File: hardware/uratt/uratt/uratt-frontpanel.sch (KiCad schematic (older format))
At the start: 17 parts

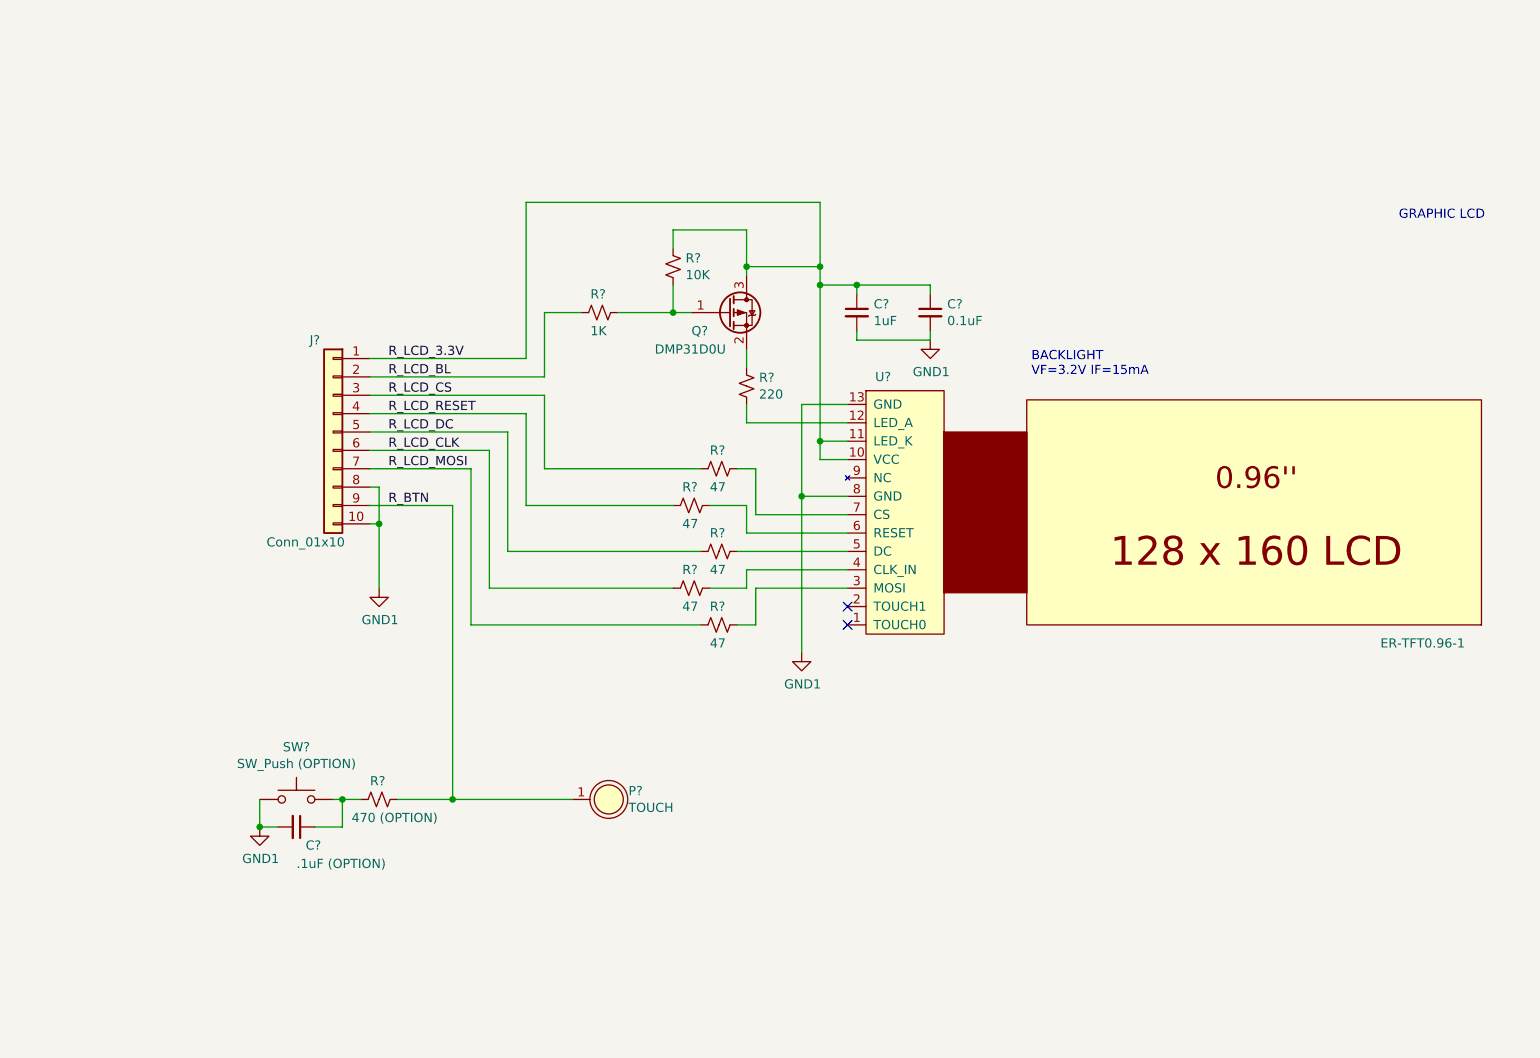
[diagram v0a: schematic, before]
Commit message: uRATT rough footprint assignment and placement for fitment
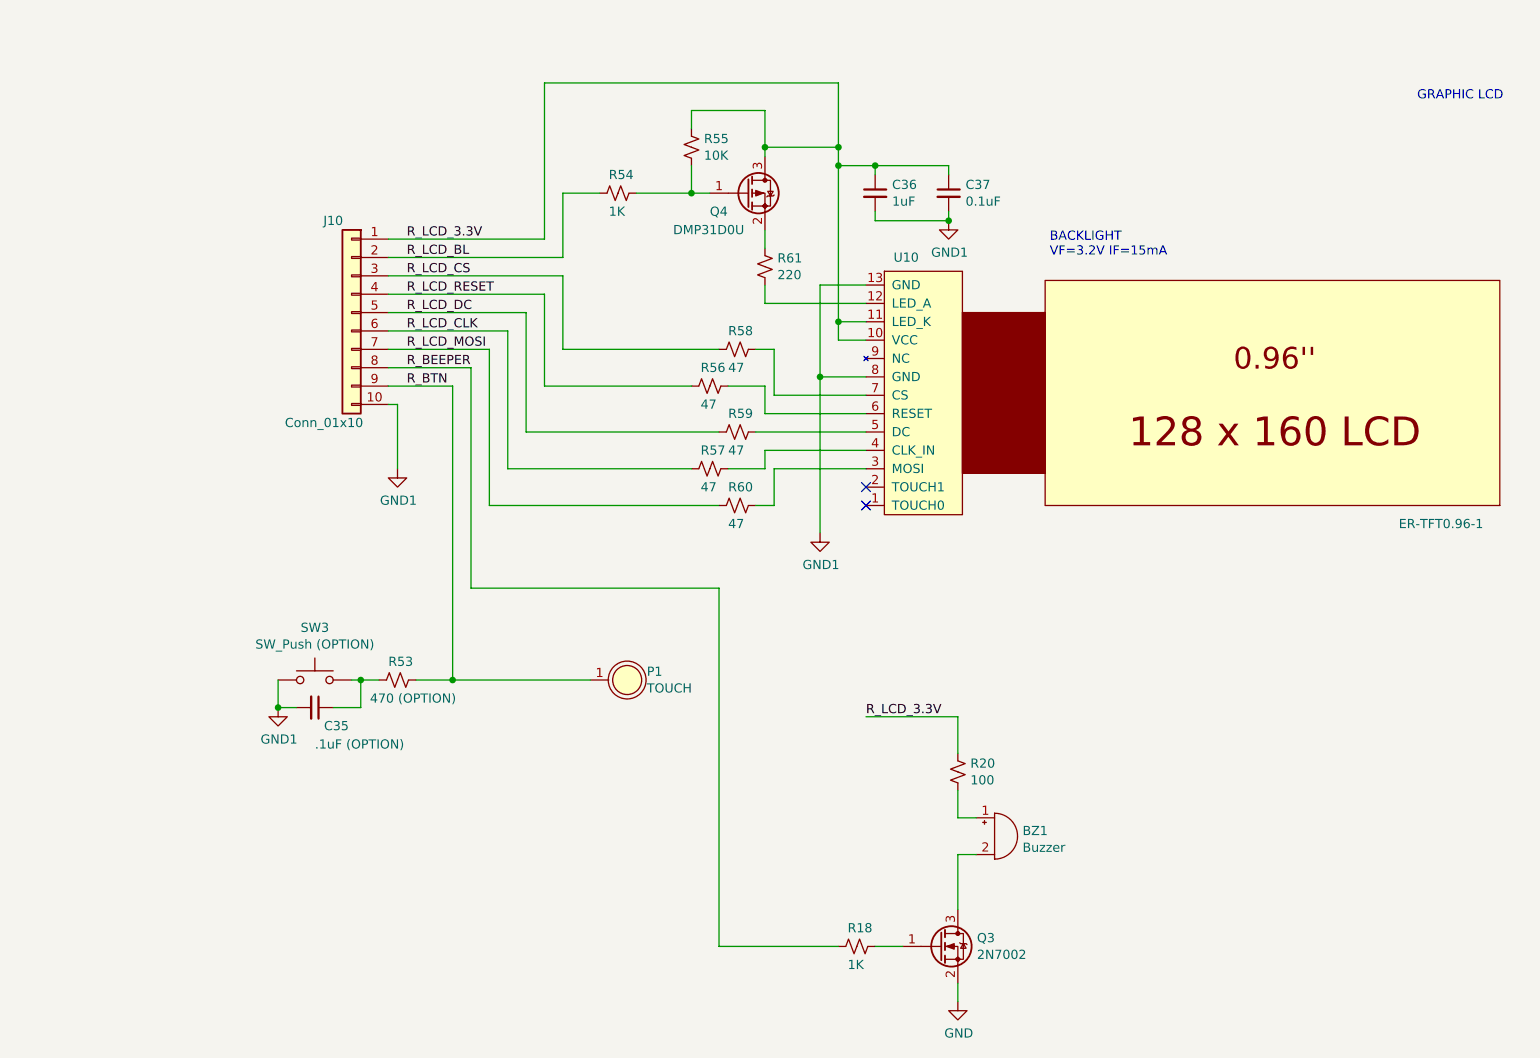
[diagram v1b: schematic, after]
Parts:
- added BZ1: Buzzer, Buzzer_Beeper:Buzzer_CUI_CPT-9019S-SMT, symbol Device:Buzzer
- added Q3: 2N7002, Package_TO_SOT_SMD:SOT-23, symbol Transistor_FET:2N7002
- added R18: 1K, Resistor_SMD:R_0603_1608Metric, symbol Device:R_Small_US
- added R20: 100, Resistor_SMD:R_0603_1608Metric, symbol Device:R_Small_US
- C35, C36, C37: renamed from C?; footprint (none) -> Capacitor_SMD:C_0603_1608Metric
- J10: renamed from J?; footprint (none) -> Connector_PinHeader_2.54mm:PinHeader_1x10_P2.54mm_Vertical
- P1: renamed from P?; footprint (none) -> TestPoint:TestPoint_Pad_4.0x4.0mm
- R53, R54, R55, R56, R57, R58, R59, R60, R61: renamed from R?; footprint (none) -> Resistor_SMD:R_0603_1608Metric
- SW3: renamed from SW?; footprint (none) -> Button_Switch_SMD:SW_Push_1P1T_NO_CK_KMR2
- gave numbers to parts that had none: 2
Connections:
- net GND1: no longer J10.8 (Pin_8)
- net R_LCD_3.3V: now also R20.1
- new net: BZ1.1 (-), R20.2
- new net: BZ1.2 (+), Q3.3 (D)
- new net: Q3.1 (G), R18.1
- new net GND: Q3.2 (S)
- new net R_BEEPER: J10.8 (Pin_8), R18.2
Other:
- moved on the sheet: C35, C36, C37, J10, P1, Q4, R53, R54, R55, R56, R57, R58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

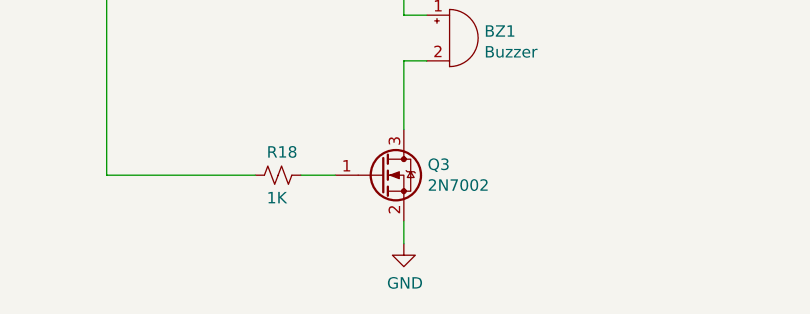
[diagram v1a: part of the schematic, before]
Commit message: import actual board outline DXF and adjust rough placement
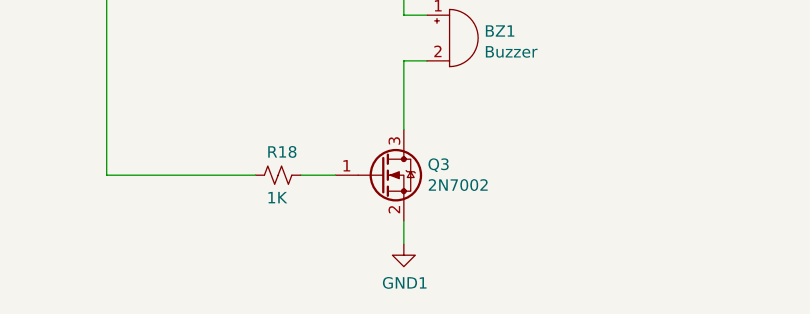
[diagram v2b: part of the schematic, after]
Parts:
- J10: footprint Connector_PinHeader_2.54mm:PinHeader_1x10_P2.54mm_Vertical -> Connector_PinHeader_2.00mm:PinHeader_1x10_P2.00mm_Vertical
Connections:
- net GND is gone; now on net GND1: Q3.2 (S)
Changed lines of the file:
@@
 F 0 "J10" H 3000 3150 50  0000 C CNN
 F 1 "Conn_01x10" H 3050 2050 50  0000 C CNN
-F 2 "Connector_PinHeader_2.54mm:PinHeader_1x10_P2.54mm_Vertical" H 2900 2650 50  0001 C CNN
+F 2 "Connector_PinHeader_2.00mm:PinHeader_1x10_P2.00mm_Vertical" H 2900 2650 50  0001 C CNN
 F 3 "~" H 2900 2650 50  0001 C CNN
 	1    2900 2650
@@
 	1    0    0    -1
 $EndComp
-$Comp
-L power:GND #PWR?
-U 1 1 60451D87
-P 6200 6400
-AR Path="/60451D87" Ref="#PWR?"  Part="1"
-AR Path="/62EF036B/60451D87" Ref="#PWR023"  Part="1"
-F 0 "#PWR023" H 6200 6150 50  0001 C CNN
-F 1 "GND" H 6205 6227 50  0000 C CNN
-F 2 "" H 6200 6400 50  0001 C CNN
-F 3 "" H 6200 6400 50  0001 C CNN
-	1    6200 6400
-	1    0    0    -1
-$EndComp
 Wire Wire Line
 	6200 6400 6200 6300
@@
 	6200 4850 6200 5050
 Connection ~ 6150 2150
+$Comp
+L power:GND1 #PWR?
+U 1 1 5FE7C0E9
+P 6200 6400
+AR Path="/5FE7C0E9" Ref="#PWR?"  Part="1"
+AR Path="/62EF036B/5FE7C0E9" Ref="#PWR?"  Part="1"
+F 0 "#PWR?" H 6200 6150 50  0001 C CNN
+F 1 "GND1" H 6205 6227 50  0000 C CNN
+F 2 "" H 6200 6400 50  0001 C CNN
+F 3 "" H 6200 6400 50  0001 C CNN
+	1    6200 6400
+	1    0    0    -1
+$EndComp
 $EndSCHEMATC

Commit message: WIP routing
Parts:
- added H5, H6, H7, H8: MountingHole, MountingHole:MountingHole_2.7mm_M2.5, symbol Mechanical:MountingHole
- J9: renamed from J10; footprint Connector_PinHeader_2.00mm:PinHeader_1x10_P2.00mm_Vertical -> Connector_FFC-FPC:TE_1-1734839-0_1x10-1MP_P0.5mm_Horizontal
- LCD1: renamed from U10; footprint (none) -> uratt:ER-TFT0.96-1
- renumbered C35 to C32, C36 to C33, C37 to C34, Q4 to Q3, Q3 to Q4, R53 to R43, R54 to R44, R55 to R45, R56 to R46, R57 to R47, R58 to R48, R59 to R49, R60 to R50, R61 to R51, R18 to R52, R20 to R53
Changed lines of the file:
@@
 $EndDescr
 $Comp
-L uratt:ER-TFT0.96-1 U?
+L uratt:ER-TFT0.96-1 LCD?
 U 1 1 62F12C4B
 P 5800 2300
-AR Path="/62F12C4B" Ref="U?"  Part="1"
-AR Path="/62EF036B/62F12C4B" Ref="U10"  Part="1"
-F 0 "U10" H 5850 2250 50  0000 L CNN
+AR Path="/62F12C4B" Ref="LCD?"  Part="1"
+AR Path="/62EF036B/62F12C4B" Ref="LCD1"  Part="1"
+F 0 "LCD1" H 5800 2250 50  0000 L CNN
 F 1 "ER-TFT0.96-1" H 8600 800 50  0000 L CNN
-F 2 "" H 5750 2375 50  0001 C CNN
+F 2 "uratt:ER-TFT0.96-1" H 5750 2375 50  0001 C CNN
 F 3 "https://www.buydisplay.com/download/manual/ER-TFT0.96-1_Datasheet.pdf" H 5750 2375 50  0001 C CNN
 	1    5800 2300
@@
 P 6150 2000
 AR Path="/62F12C53" Ref="C?"  Part="1"
-AR Path="/62EF036B/62F12C53" Ref="C37"  Part="1"
-F 0 "C37" H 6242 2046 50  0000 L CNN
+AR Path="/62EF036B/62F12C53" Ref="C34"  Part="1"
+F 0 "C34" H 6242 2046 50  0000 L CNN
 F 1 "0.1uF" H 6242 1955 50  0000 L CNN
 F 2 "Capacitor_SMD:C_0603_1608Metric" H 6150 2000 50  0001 C CNN
@@
 P 5750 2000
 AR Path="/62F12C5A" Ref="C?"  Part="1"
-AR Path="/62EF036B/62F12C5A" Ref="C36"  Part="1"
-F 0 "C36" H 5842 2046 50  0000 L CNN
+AR Path="/62EF036B/62F12C5A" Ref="C33"  Part="1"
+F 0 "C33" H 5842 2046 50  0000 L CNN
 F 1 "1uF" H 5842 1955 50  0000 L CNN
 F 2 "Capacitor_SMD:C_0603_1608Metric" H 5750 2000 50  0001 C CNN
@@
 P 5050 2000
 AR Path="/62F12C68" Ref="Q?"  Part="1"
-AR Path="/62EF036B/62F12C68" Ref="Q4"  Part="1"
-F 0 "Q4" H 4850 1900 50  0000 L CNN
+AR Path="/62EF036B/62F12C68" Ref="Q3"  Part="1"
+F 0 "Q3" H 4850 1900 50  0000 L CNN
 F 1 "DMP31D0U" H 4650 1800 50  0000 L CNN
 F 2 "Package_TO_SOT_SMD:SOT-23" H 5250 1925 50  0001 L CIN
@@
 P 5150 2400
 AR Path="/62F12C6E" Ref="R?"  Part="1"
-AR Path="/62EF036B/62F12C6E" Ref="R61"  Part="1"
-F 0 "R61" H 5218 2446 50  0000 L CNN
+AR Path="/62EF036B/62F12C6E" Ref="R51"  Part="1"
+F 0 "R51" H 5218 2446 50  0000 L CNN
 F 1 "220" H 5218 2355 50  0000 L CNN
 F 2 "Resistor_SMD:R_0603_1608Metric" H 5150 2400 50  0001 C CNN
@@
 P 4750 1750
 AR Path="/62F12C84" Ref="R?"  Part="1"
-AR Path="/62EF036B/62F12C84" Ref="R55"  Part="1"
-F 0 "R55" H 4818 1796 50  0000 L CNN
+AR Path="/62EF036B/62F12C84" Ref="R45"  Part="1"
+F 0 "R45" H 4818 1796 50  0000 L CNN
 F 1 "10K" H 4818 1705 50  0000 L CNN
 F 2 "Resistor_SMD:R_0603_1608Metric" H 4750 1750 50  0001 C CNN
@@
 P 5000 2850
 AR Path="/62F12C96" Ref="R?"  Part="1"
-AR Path="/62EF036B/62F12C96" Ref="R58"  Part="1"
-F 0 "R58" V 4900 2800 50  0000 L CNN
+AR Path="/62EF036B/62F12C96" Ref="R48"  Part="1"
+F 0 "R48" V 4900 2800 50  0000 L CNN
 F 1 "47" V 5100 2800 50  0000 L CNN
 F 2 "Resistor_SMD:R_0603_1608Metric" H 5000 2850 50  0001 C CNN
@@
 P 4850 3050
 AR Path="/62F12C9C" Ref="R?"  Part="1"
-AR Path="/62EF036B/62F12C9C" Ref="R56"  Part="1"
-F 0 "R56" V 4750 3000 50  0000 L CNN
+AR Path="/62EF036B/62F12C9C" Ref="R46"  Part="1"
+F 0 "R46" V 4750 3000 50  0000 L CNN
 F 1 "47" V 4950 3000 50  0000 L CNN
 F 2 "Resistor_SMD:R_0603_1608Metric" H 4850 3050 50  0001 C CNN
@@
 P 5000 3300
 AR Path="/62F12CA2" Ref="R?"  Part="1"
-AR Path="/62EF036B/62F12CA2" Ref="R59"  Part="1"
-F 0 "R59" V 4900 3250 50  0000 L CNN
+AR Path="/62EF036B/62F12CA2" Ref="R49"  Part="1"
+F 0 "R49" V 4900 3250 50  0000 L CNN
 F 1 "47" V 5100 3250 50  0000 L CNN
 F 2 "Resistor_SMD:R_0603_1608Metric" H 5000 3300 50  0001 C CNN
@@
 P 4850 3500
 AR Path="/62F12CA8" Ref="R?"  Part="1"
-AR Path="/62EF036B/62F12CA8" Ref="R57"  Part="1"
-F 0 "R57" V 4750 3450 50  0000 L CNN
+AR Path="/62EF036B/62F12CA8" Ref="R47"  Part="1"
+F 0 "R47" V 4750 3450 50  0000 L CNN
 F 1 "47" V 4950 3450 50  0000 L CNN
 F 2 "Resistor_SMD:R_0603_1608Metric" H 4850 3500 50  0001 C CNN
@@
 P 5000 3700
 AR Path="/62F12CAE" Ref="R?"  Part="1"
-AR Path="/62EF036B/62F12CAE" Ref="R60"  Part="1"
-F 0 "R60" V 4900 3650 50  0000 L CNN
+AR Path="/62EF036B/62F12CAE" Ref="R50"  Part="1"
+F 0 "R50" V 4900 3650 50  0000 L CNN
 F 1 "47" V 5100 3650 50  0000 L CNN
 F 2 "Resistor_SMD:R_0603_1608Metric" H 5000 3700 50  0001 C CNN
@@
 P 4350 2000
 AR Path="/62F12CC0" Ref="R?"  Part="1"
-AR Path="/62EF036B/62F12CC0" Ref="R54"  Part="1"
-F 0 "R54" V 4250 1950 50  0000 L CNN
+AR Path="/62EF036B/62F12CC0" Ref="R44"  Part="1"
+F 0 "R44" V 4250 1950 50  0000 L CNN
 F 1 "1K" V 4450 1950 50  0000 L CNN
 F 2 "Resistor_SMD:R_0603_1608Metric" H 4350 2000 50  0001 C CNN
@@
 P 2900 2650
 AR Path="/62F12CC7" Ref="J?"  Part="1"
-AR Path="/62EF036B/62F12CC7" Ref="J10"  Part="1"
-F 0 "J10" H 3000 3150 50  0000 C CNN
+AR Path="/62EF036B/62F12CC7" Ref="J9"  Part="1"
+F 0 "J9" H 3000 3150 50  0000 C CNN
 F 1 "Conn_01x10" H 3050 2050 50  0000 C CNN
-F 2 "Connector_PinHeader_2.00mm:PinHeader_1x10_P2.00mm_Vertical" H 2900 2650 50  0001 C CNN
+F 2 "Connector_FFC-FPC:TE_1-1734839-0_1x10-1MP_P0.5mm_Horizontal" H 2900 2650 50  0001 C CNN
 F 3 "~" H 2900 2650 50  0001 C CNN
 	1    2900 2650
@@
 P 3150 3500
 AR Path="/62F12CDD" Ref="#PWR?"  Part="1"
-AR Path="/62EF036B/62F12CDD" Ref="#PWR099"  Part="1"
-F 0 "#PWR099" H 3150 3250 50  0001 C CNN
+AR Path="/62EF036B/62F12CDD" Ref="#PWR091"  Part="1"
+F 0 "#PWR091" H 3150 3250 50  0001 C CNN
 F 1 "GND1" H 3155 3327 50  0000 C CNN
 F 2 "" H 3150 3500 50  0001 C CNN
@@
 P 6150 2150
 AR Path="/62F12CE5" Ref="#PWR?"  Part="1"
-AR Path="/62EF036B/62F12CE5" Ref="#PWR0101"  Part="1"
-F 0 "#PWR0101" H 6150 1900 50  0001 C CNN
+AR Path="/62EF036B/62F12CE5" Ref="#PWR093"  Part="1"
+F 0 "#PWR093" H 6150 1900 50  0001 C CNN
 F 1 "GND1" H 6155 1977 50  0000 C CNN
 F 2 "" H 6150 2150 50  0001 C CNN
@@
 P 5450 3850
 AR Path="/62F12CEB" Ref="#PWR?"  Part="1"
-AR Path="/62EF036B/62F12CEB" Ref="#PWR0100"  Part="1"
-F 0 "#PWR0100" H 5450 3600 50  0001 C CNN
+AR Path="/62EF036B/62F12CEB" Ref="#PWR092"  Part="1"
+F 0 "#PWR092" H 5450 3600 50  0001 C CNN
 F 1 "GND1" H 5455 3677 50  0000 C CNN
 F 2 "" H 5450 3850 50  0001 C CNN
@@
 P 3150 4650
 AR Path="/6319A3AD" Ref="R?"  Part="1"
-AR Path="/62EF036B/6319A3AD" Ref="R53"  Part="1"
-F 0 "R53" V 3050 4600 50  0000 L CNN
+AR Path="/62EF036B/6319A3AD" Ref="R43"  Part="1"
+F 0 "R43" V 3050 4600 50  0000 L CNN
 F 1 "470 (OPTION)" V 3250 4500 50  0000 L CNN
 F 2 "Resistor_SMD:R_0603_1608Metric" H 3150 4650 50  0001 C CNN
@@
 P 2700 4800
 AR Path="/6319A3BE" Ref="C?"  Part="1"
-AR Path="/62EF036B/6319A3BE" Ref="C35"  Part="1"
-F 0 "C35" V 2800 4850 50  0000 L CNN
+AR Path="/62EF036B/6319A3BE" Ref="C32"  Part="1"
+F 0 "C32" V 2800 4850 50  0000 L CNN
 F 1 ".1uF (OPTION)" V 2900 4800 50  0000 L CNN
 F 2 "Capacitor_SMD:C_0603_1608Metric" H 2700 4800 50  0001 C CNN
@@
 P 2500 4800
 AR Path="/6319ECB9" Ref="#PWR?"  Part="1"
-AR Path="/62EF036B/6319ECB9" Ref="#PWR098"  Part="1"
-F 0 "#PWR098" H 2500 4550 50  0001 C CNN
+AR Path="/62EF036B/6319ECB9" Ref="#PWR090"  Part="1"
+F 0 "#PWR090" H 2500 4550 50  0001 C CNN
 F 1 "GND1" H 2505 4627 50  0000 C CNN
 F 2 "" H 2500 4800 50  0001 C CNN
@@
 P 6100 6100
 AR Path="/60451D78" Ref="Q?"  Part="1"
-AR Path="/62EF036B/60451D78" Ref="Q3"  Part="1"
-F 0 "Q3" H 6304 6146 50  0000 L CNN
+AR Path="/62EF036B/60451D78" Ref="Q4"  Part="1"
+F 0 "Q4" H 6304 6146 50  0000 L CNN
 F 1 "2N7002" H 6304 6055 50  0000 L CNN
 F 2 "Package_TO_SOT_SMD:SOT-23" H 6300 6025 50  0001 L CIN
@@
 P 6200 5150
 AR Path="/60451D80" Ref="R?"  Part="1"
-AR Path="/62EF036B/60451D80" Ref="R20"  Part="1"
-F 0 "R20" H 6268 5196 50  0000 L CNN
+AR Path="/62EF036B/60451D80" Ref="R53"  Part="1"
+F 0 "R53" H 6268 5196 50  0000 L CNN
 F 1 "100" H 6268 5105 50  0000 L CNN
 F 2 "Resistor_SMD:R_0603_1608Metric" H 6200 5150 50  0001 C CNN
@@
 P 5650 6100
 AR Path="/60451D8E" Ref="R?"  Part="1"
-AR Path="/62EF036B/60451D8E" Ref="R18"  Part="1"
-F 0 "R18" V 5550 6050 50  0000 L CNN
+AR Path="/62EF036B/60451D8E" Ref="R52"  Part="1"
+F 0 "R52" V 5550 6050 50  0000 L CNN
 F 1 "1K" V 5750 6050 50  0000 L CNN
 F 2 "Resistor_SMD:R_0603_1608Metric" H 5650 6100 50  0001 C CNN
@@
 P 6200 6400
 AR Path="/5FE7C0E9" Ref="#PWR?"  Part="1"
-AR Path="/62EF036B/5FE7C0E9" Ref="#PWR?"  Part="1"
-F 0 "#PWR?" H 6200 6150 50  0001 C CNN
+AR Path="/62EF036B/5FE7C0E9" Ref="#PWR094"  Part="1"
+F 0 "#PWR094" H 6200 6150 50  0001 C CNN
 F 1 "GND1" H 6205 6227 50  0000 C CNN
 F 2 "" H 6200 6400 50  0001 C CNN
@@
 	1    0    0    -1
 $EndComp
+$Comp
+L Mechanical:MountingHole H?
+U 1 1 5FEBDB85
+P 8150 4550
+AR Path="/61FC99B5/5FEBDB85" Ref="H?"  Part="1"
+AR Path="/62EF036B/5FEBDB85" Ref="H5"  Part="1"
+F 0 "H5" H 8250 4596 50  0000 L CNN
+F 1 "MountingHole" H 8250 4505 50  0000 L CNN
+F 2 "MountingHole:MountingHole_2.7mm_M2.5" H 8150 4550 50  0001 C CNN
+F 3 "~" H 8150 4550 50  0001 C CNN
+	1    8150 4550
+	1    0    0    -1
+$EndComp
+$Comp
+L Mechanical:MountingHole H?
+U 1 1 5FEBDB8B
+P 8150 4800
+AR Path="/61FC99B5/5FEBDB8B" Ref="H?"  Part="1"
+AR Path="/62EF036B/5FEBDB8B" Ref="H6"  Part="1"
+F 0 "H6" H 8250 4846 50  0000 L CNN
+F 1 "MountingHole" H 8250 4755 50  0000 L CNN
+F 2 "MountingHole:MountingHole_2.7mm_M2.5" H 8150 4800 50  0001 C CNN
+F 3 "~" H 8150 4800 50  0001 C CNN
+	1    8150 4800
+	1    0    0    -1
+$EndComp
+$Comp
+L Mechanical:MountingHole H?
+U 1 1 5FEBDB91
+P 8150 5050
+AR Path="/61FC99B5/5FEBDB91" Ref="H?"  Part="1"
+AR Path="/62EF036B/5FEBDB91" Ref="H7"  Part="1"
+F 0 "H7" H 8250 5096 50  0000 L CNN
+F 1 "MountingHole" H 8250 5005 50  0000 L CNN
+F 2 "MountingHole:MountingHole_2.7mm_M2.5" H 8150 5050 50  0001 C CNN
+F 3 "~" H 8150 5050 50  0001 C CNN
+	1    8150 5050
+	1    0    0    -1
+$EndComp
+$Comp
+L Mechanical:MountingHole H?
+U 1 1 5FEBDB97
+P 8150 5300
+AR Path="/61FC99B5/5FEBDB97" Ref="H?"  Part="1"
+AR Path="/62EF036B/5FEBDB97" Ref="H8"  Part="1"
+F 0 "H8" H 8250 5346 50  0000 L CNN
+F 1 "MountingHole" H 8250 5255 50  0000 L CNN
+F 2 "MountingHole:MountingHole_2.7mm_M2.5" H 8150 5300 50  0001 C CNN
+F 3 "~" H 8150 5300 50  0001 C CNN
+	1    8150 5300
+	1    0    0    -1
+$EndComp
